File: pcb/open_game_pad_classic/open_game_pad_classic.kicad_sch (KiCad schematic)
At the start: 41 parts, among them J1 COM-09032, J2 COM-09032, U1 MM74C923, U2 74HC4051, U3 SN74AHC1G04DBVR, U4 LM358

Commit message: Updated the PCB and scheme. 2-layered, ground plane.
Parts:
- removed U4: LM358, LM358:DIL8, symbol Amplifier_Operational:LM358
- added AMP1: LM358, LM358:DIL8, symbol LM358:LM358
- C1: footprint Capacitor_SMD:C_0603_1608Metric -> Capacitor_SMD:C_0201_0603Metric
- C2, C3: footprint Capacitor_SMD:C_0402_1005Metric -> Capacitor_SMD:C_0201_0603Metric
- R1: footprint Resistor_SMD:R_0603_1608Metric -> Resistor_SMD:R_0402_1005Metric
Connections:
- net AIN: now also AMP1.1
- net at R10.2, R7.1: now also AMP1.2
- net at R8.2, R9.1: now also AMP1.3
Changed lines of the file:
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@@
 	)
 	(junction
+		(at 137.16 115.57)
+		(diameter 0)
+		(color 0 0 0 0)
+	)
+	(junction
 		(at 80.01 66.04)
 		(diameter 0)
@@
 	)
 	(junction
-		(at 137.16 115.57)
-		(diameter 0)
-		(color 0 0 0 0)
-	)
-	(junction
 		(at 60.96 121.92)
 		(diameter 0)
@@
 	)
 	(symbol
-		(lib_id "custom:SW_SPST_45_DEG")
-		(at 69.85 228.6 0)
+		(lib_id "LM358:LM358")
+		(at 129.54 115.57 0)
 		(unit 1)
 		(exclude_from_sim no)
@@
 		(dnp no)
 		(fields_autoplaced yes)
-		(property "Reference" "SW4"
-			(at 69.85 220.98 0)
+		(property "Reference" "AMP1"
+			(at 129.54 105.41 0)
 			(effects
 				(font
@@
 			)
 		)
-		(property "Value" "~"
-			(at 69.85 223.52 0)
+		(property "Value" "LM358"
+			(at 129.54 107.95 0)
 			(effects
 				(font
@@
 			)
 		)
-		(property "Footprint" "TS02-66-95-BK-260-LCR-D:SW_TS02-66-95-BK-260-LCR-D"
-			(at 69.85 228.6 0)
+		(property "Footprint" "LM358:DIL8"
+			(at 129.54 115.57 0)
 			(effects
 				(font
 					(size 1.27 1.27)
 				)
+				(justify bottom)
 				(hide yes)
 			)
 		)
-		(property "Datasheet" "~"
-			(at 69.85 228.6 0)
+		(property "Datasheet" ""
+			(at 129.54 115.57 0)
 			(effects
 				(font
@@
 			)
 		)
-		(property "Description" "Single Pole Single Throw (SPST) switch 45 deg"
-			(at 70.358 228.6 0)
+		(property "Description" ""
+			(at 129.54 115.57 0)
 			(effects
 				(font
@@
 			)
 		)
-		(pin "2"
+		(property "MF" "Texas Instruments"
+			(at 129.54 115.57 0)
+			(effects
+				(font
+					(size 1.27 1.27)
+				)
+				(justify bottom)
+				(hide yes)
+			)
 		)
-		(pin "1"
+		(property "Description_1" "\nOp Amp Dual Low Power Amplifier ±16V/32V 8-Pin TO-99 Tube\n"
+			(at 129.54 115.57 0)
+			(effects
+				(font
+					(size 1.27 1.27)
+				)
+				(justify bottom)
+				(hide yes)
+			)
 		)
-		(pin "3"
+		(property "Package" "None"
+			(at 129.54 115.57 0)
+			(effects
+				(font
+					(size 1.27 1.27)
+				)
+				(justify bottom)
+				(hide yes)
+			)
+		)
+		(property "Price" "None"
+			(at 129.54 115.57 0)
+			(effects
+				(font
+					(size 1.27 1.27)
+				)
+				(justify bottom)
+				(hide yes)
+			)
+		)
+		(property "SnapEDA_Link" "https://www.snapeda.com/parts/LM358/Texas+Instruments/view-part/?ref=snap"
+			(at 129.54 115.57 0)
+			(effects
+				(font
+					(size 1.27 1.27)
+				)
+				(justify bottom)
+				(hide yes)
+			)
+		)
+		(property "MP" "LM358"
+			(at 129.54 115.57 0)
+			(effects
+				(font
+					(size 1.27 1.27)
+				)
+				(justify bottom)
+				(hide yes)
+			)
+		)
+		(property "Purchase-URL" "https://www.snapeda.com/api/url_track_click_mouser/?unipart_id=11831622&manufacturer=Texas Instruments&part_name=LM358&search_term=None"
+			(at 129.54 115.57 0)
+			(effects
+				(font
+					(size 1.27 1.27)
+				)
+				(justify bottom)
+				(hide yes)
+			)
+		)
+		(property "Availability" "Not in stock"
+			(at 129.54 115.57 0)
+			(effects
+				(font
+					(size 1.27 1.27)
+				)
+				(justify bottom)
+				(hide yes)
+			)
+		)
+		(property "Check_prices" "https://www.snapeda.com/parts/LM358/Texas+Instruments/view-part/?ref=eda"
+			(at 129.54 115.57 0)
+			(effects
+				(font
+					(size 1.27 1.27)
+				)
+				(justify bottom)
+				(hide yes)
+			)
+		)
+		(pin "8"
 		)
 		(pin "4"
 		)
+		(pin "5"
+		)
+		(pin "6"
+		)
+		(pin "7"
+		)
+		(pin "1"
+		)
+		(pin "2"
+		)
+		(pin "3"
+		)
 		(instances
 			(project "open_game_pad_classic"
 				(path "/49f049bd-a8cc-4b05-820e-5d41d7ecc0be"
-					(reference "SW4")
+					(reference "AMP1")
 					(unit 1)
 				)
@@
 	(symbol
 		(lib_id "custom:SW_SPST_45_DEG")
-		(at 35.56 217.17 0)
+		(at 69.85 228.6 0)
 		(unit 1)
 		(exclude_from_sim no)
@@
 		(dnp no)
 		(fields_autoplaced yes)
-		(property "Reference" "SW5"
-			(at 35.56 209.55 0)
+		(property "Reference" "SW4"
+			(at 69.85 220.98 0)
 			(effects
 				(font
@@
 		)
 		(property "Value" "~"
-			(at 35.56 212.09 0)
+			(at 69.85 223.52 0)
 			(effects
 				(font
@@
 		)
 		(property "Footprint" "TS02-66-95-BK-260-LCR-D:SW_TS02-66-95-BK-260-LCR-D"
-			(at 35.56 217.17 0)
+			(at 69.85 228.6 0)
 			(effects
 				(font
@@
 		)
 		(property "Datasheet" "~"
-			(at 35.56 217.17 0)
+			(at 69.85 228.6 0)
 			(effects
 				(font
@@
 		)
 		(property "Description" "Single Pole Single Throw (SPST) switch 45 deg"
-			(at 36.068 217.17 0)
+			(at 70.358 228.6 0)
 			(effects
 				(font
@@
 		(pin "1"
 		)
-		(pin "4"
-		)
 		(pin "3"
 		)
+		(pin "4"
+		)
 		(instances
 			(project "open_game_pad_classic"
 				(path "/49f049bd-a8cc-4b05-820e-5d41d7ecc0be"
-					(reference "SW5")
+					(reference "SW4")
 					(unit 1)
 				)
@@
 	(symbol
 		(lib_id "custom:SW_SPST_45_DEG")
-		(at 46.99 205.74 0)
+		(at 35.56 217.17 0)
 		(unit 1)
 		(exclude_from_sim no)
@@
 		(dnp no)
 		(fields_autoplaced yes)
-		(property "Reference" "SW10"
-			(at 46.99 198.12 0)
+		(property "Reference" "SW5"
+			(at 35.56 209.55 0)
 			(effects
 				(font
@@
 		)
 		(property "Value" "~"
-			(at 46.99 200.66 0)
+			(at 35.56 212.09 0)
 			(effects
 				(font
@@
 		)
 		(property "Footprint" "TS02-66-95-BK-260-LCR-D:SW_TS02-66-95-BK-260-LCR-D"
-			(at 46.99 205.74 0)
+			(at 35.56 217.17 0)
 			(effects
 				(font
@@
 		)
 		(property "Datasheet" "~"
-			(at 46.99 205.74 0)
+			(at 35.56 217.17 0)
 			(effects
 				(font
@@
 		)
 		(property "Description" "Single Pole Single Throw (SPST) switch 45 deg"
-			(at 47.498 205.74 0)
+			(at 36.068 217.17 0)
 			(effects
 				(font
@@
 			(project "open_game_pad_classic"
 				(path "/49f049bd-a8cc-4b05-820e-5d41d7ecc0be"
-					(reference "SW10")
+					(reference "SW5")
 					(unit 1)
 				)
@@
 	(symbol
 		(lib_id "custom:SW_SPST_45_DEG")
-		(at 58.42 194.31 0)
+		(at 46.99 205.74 0)
 		(unit 1)
 		(exclude_from_sim no)
@@
 		(dnp no)
 		(fields_autoplaced yes)
-		(property "Reference" "SW15"
-			(at 58.42 186.69 0)
+		(property "Reference" "SW10"
+			(at 46.99 198.12 0)
 			(effects
 				(font
@@
 		)
 		(property "Value" "~"
-			(at 58.42 189.23 0)
+			(at 46.99 200.66 0)
 			(effects
 				(font
@@
 		)
 		(property "Footprint" "TS02-66-95-BK-260-LCR-D:SW_TS02-66-95-BK-260-LCR-D"
-			(at 58.42 194.31 0)
+			(at 46.99 205.74 0)
 			(effects
 				(font
@@
 		)
 		(property "Datasheet" "~"
-			(at 58.42 194.31 0)
+			(at 46.99 205.74 0)
 			(effects
 				(font
@@
 		)
 		(property "Description" "Single Pole Single Throw (SPST) switch 45 deg"
-			(at 58.928 194.31 0)
+			(at 47.498 205.74 0)
 			(effects
 				(font
@@
 			(project "open_game_pad_classic"
 				(path "/49f049bd-a8cc-4b05-820e-5d41d7ecc0be"
-					(reference "SW15")
+					(reference "SW10")
 					(unit 1)
 				)
@@
 	)
 	(symbol
-		(lib_id "Amplifier_Operational:LM358")
-		(at 129.54 115.57 0)
+		(lib_id "custom:SW_SPST_45_DEG")
+		(at 58.42 194.31 0)
 		(unit 1)
 		(exclude_from_sim no)
@@
 		(on_board yes)
 		(dnp no)
-		(property "Reference" "U4"
-			(at 129.54 105.41 0)
+		(fields_autoplaced yes)
+		(property "Reference" "SW15"
+			(at 58.42 186.69 0)
 			(effects
 				(font
@@
 			)
 		)
-		(property "Value" "LM358"
-			(at 129.54 107.95 0)
+		(property "Value" "~"
+			(at 58.42 189.23 0)
 			(effects
 				(font
@@
 			)
 		)
-		(property "Footprint" "LM358:DIL8"
-			(at 129.54 115.57 0)
+		(property "Footprint" "TS02-66-95-BK-260-LCR-D:SW_TS02-66-95-BK-260-LCR-D"
+			(at 58.42 194.31 0)
 			(effects
 				(font
@@
 			)
 		)
-		(property "Datasheet" "http://www.ti.com/lit/ds/symlink/lm2904-n.pdf"
-			(at 129.54 115.57 0)
+		(property "Datasheet" "~"
+			(at 58.42 194.31 0)
 			(effects
 				(font
@@
 			)
 		)
-		(property "Description" "Low-Power, Dual Operational Amplifiers, DIP-8/SOIC-8/TO-99-8"
-			(at 129.54 115.57 0)
+		(property "Description" "Single Pole Single Throw (SPST) switch 45 deg"
+			(at 58.928 194.31 0)
 			(effects
 				(font
@@
 			)
 		)
-		(pin "1"
-		)
-		(pin "8"
-		)
-		(pin "5"
-		)
-		(pin "3"
-		)
-		(pin "6"
-		)
 		(pin "2"
 		)
-		(pin "7"
+		(pin "1"
 		)
 		(pin "4"
 		)
+		(pin "3"
+		)
 		(instances
 			(project "open_game_pad_classic"
 				(path "/49f049bd-a8cc-4b05-820e-5d41d7ecc0be"
-					(reference "U4")
+					(reference "SW15")
 					(unit 1)
 				)
@@
 			)
 		)
-		(property "Footprint" "Capacitor_SMD:C_0402_1005Metric"
+		(property "Footprint" "Capacitor_SMD:C_0201_0603Metric"
 			(at 135.89 235.9152 0)
 			(effects
@@
 			)
 		)
-		(property "Footprint" "Resistor_SMD:R_0603_1608Metric"
+		(property "Footprint" "Resistor_SMD:R_0402_1005Metric"
 			(at 68.58 33.02 0)
 			(effects
@@
 			)
 		)
-		(property "Footprint" "Capacitor_SMD:C_0402_1005Metric"
+		(property "Footprint" "Capacitor_SMD:C_0201_0603Metric"
 			(at 127 238.4552 0)
 			(effects
@@
 			)
 		)
-		(property "Footprint" "Capacitor_SMD:C_0603_1608Metric"
+		(property "Footprint" "Capacitor_SMD:C_0201_0603Metric"
 			(at 167.3352 52.07 0)
 			(effects

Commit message: More decoupling for microcontroller and timer.
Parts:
- added C4: 10 pF, Capacitor_SMD:C_0201_0603Metric, symbol Device:C
- added C5: 10 µF, Capacitor_SMD:C_0603_1608Metric, symbol Device:C
- added C6: 100nF, Capacitor_SMD:C_0201_0603Metric, symbol Device:C
- C1: footprint Capacitor_SMD:C_0201_0603Metric -> Capacitor_SMD:C_0603_1608Metric
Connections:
- net +5V: now also C5.1, C6.1
- net CLK: now also C4.1
- net GND: now also C4.2, C5.2, C6.2
- no-connect marks 4 -> 5
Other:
- note added: "18 Tactile digital switch matrix."
- note removed: "15 Tactile digital switch matrix."
- moved on the sheet: C1

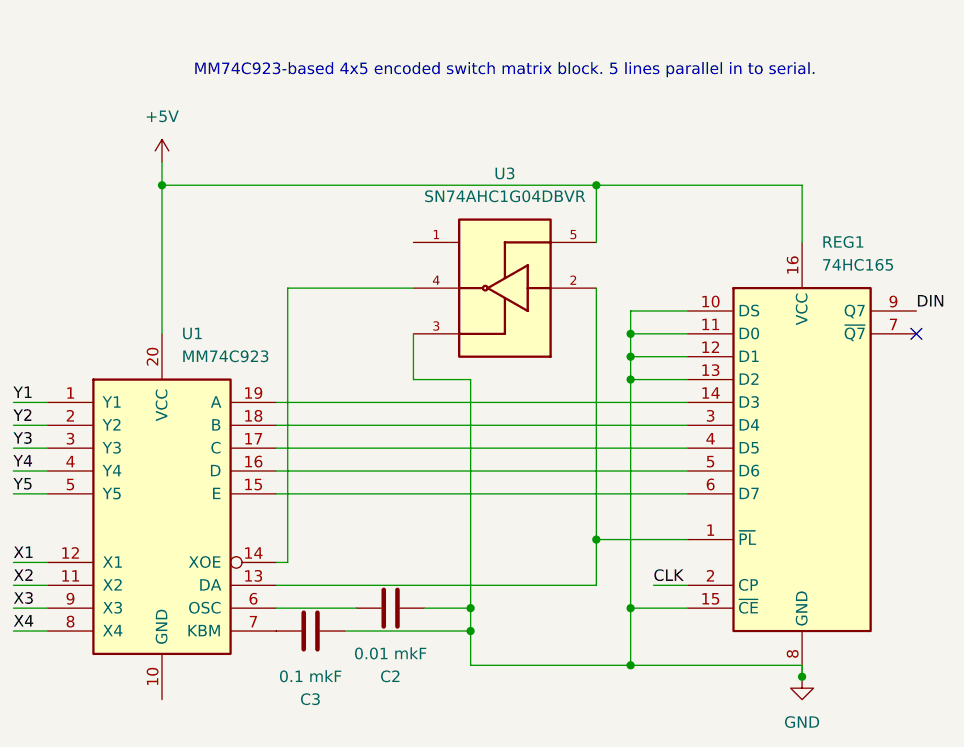
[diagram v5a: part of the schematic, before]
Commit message: Fixed the schematic on PISO read. Updated the PCB.
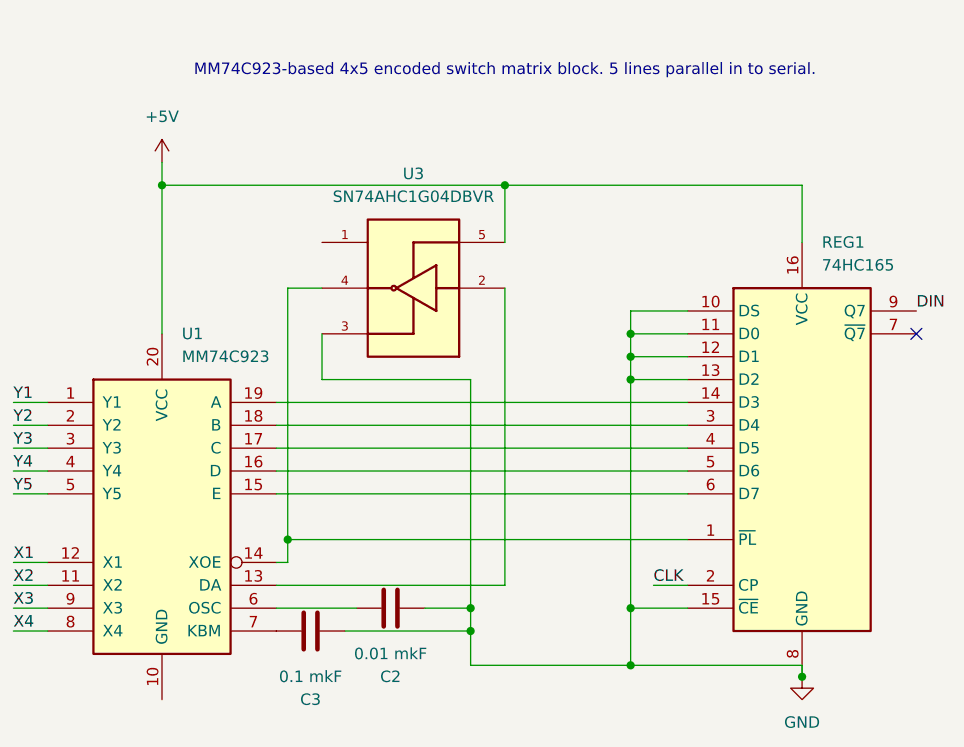
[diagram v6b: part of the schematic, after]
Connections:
- net at U1.13 (DA), U3.2: no longer REG1.1 (~{PL})
- net at U1.14 (XOE), U3.4: now also REG1.1 (~{PL})
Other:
- moved on the sheet: U3
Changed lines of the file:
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@@
 	)
 	(junction
-		(at 154.94 227.33)
-		(diameter 0)
-		(color 0 0 0 0)
-	)
-	(junction
 		(at 118.11 118.11)
 		(diameter 0)
@@
 	)
 	(junction
-		(at 140.97 234.95)
-		(diameter 0)
-		(color 0 0 0 0)
-	)
-	(junction
 		(at 74.93 231.14)
 		(diameter 0)
@@
 	)
 	(junction
+		(at 140.97 234.95)
+		(diameter 0)
+		(color 0 0 0 0)
+	)
+	(junction
 		(at 158.75 234.95)
 		(diameter 0)
@@
 	)
 	(junction
+		(at 144.78 187.96)
+		(diameter 0)
+		(color 0 0 0 0)
+	)
+	(junction
 		(at 40.64 219.71)
 		(diameter 0)
@@
 	)
 	(junction
+		(at 120.65 227.33)
+		(diameter 0)
+		(color 0 0 0 0)
+	)
+	(junction
 		(at 158.75 209.55)
 		(diameter 0)
@@
 	)
 	(junction
-		(at 154.94 187.96)
-		(diameter 0)
-		(color 0 0 0 0)
-	)
-	(junction
 		(at 76.2 135.89)
 		(diameter 0)
@@
 	(wire
 		(pts
-			(xy 106.68 187.96) (xy 154.94 187.96)
+			(xy 106.68 187.96) (xy 144.78 187.96)
 		)
 		(stroke
@@
 	(wire
 		(pts
-			(xy 140.97 209.55) (xy 140.97 234.95)
+			(xy 119.38 229.87) (xy 120.65 229.87)
 		)
 		(stroke
@@
 	(wire
 		(pts
-			(xy 119.38 229.87) (xy 120.65 229.87)
+			(xy 120.65 199.39) (xy 124.46 199.39)
 		)
 		(stroke
@@
 	(wire
 		(pts
-			(xy 120.65 199.39) (xy 134.62 199.39)
+			(xy 119.38 212.09) (xy 165.1 212.09)
 		)
 		(stroke
@@
 	(wire
 		(pts
-			(xy 119.38 212.09) (xy 165.1 212.09)
+			(xy 71.12 66.04) (xy 80.01 66.04)
 		)
 		(stroke
@@
 	(wire
 		(pts
-			(xy 71.12 66.04) (xy 80.01 66.04)
+			(xy 105.41 43.18) (xy 118.11 43.18)
 		)
 		(stroke
@@
 	(wire
 		(pts
-			(xy 105.41 43.18) (xy 118.11 43.18)
+			(xy 90.17 62.23) (xy 90.17 66.04)
 		)
 		(stroke
@@
 	(wire
 		(pts
-			(xy 90.17 62.23) (xy 90.17 66.04)
+			(xy 73.66 118.11) (xy 78.74 118.11)
 		)
 		(stroke
@@
 	(wire
 		(pts
-			(xy 73.66 118.11) (xy 78.74 118.11)
+			(xy 135.89 234.95) (xy 140.97 234.95)
 		)
 		(stroke
@@
 	(wire
 		(pts
-			(xy 140.97 209.55) (xy 134.62 209.55)
+			(xy 140.97 209.55) (xy 124.46 209.55)
 		)
 		(stroke
@@
 	(wire
 		(pts
-			(xy 63.5 153.67) (xy 49.53 153.67)
+			(xy 120.65 227.33) (xy 165.1 227.33)
 		)
 		(stroke
@@
 	(wire
 		(pts
-			(xy 180.34 125.73) (xy 180.34 123.19)
+			(xy 63.5 153.67) (xy 49.53 153.67)
 		)
 		(stroke
@@
 	(wire
 		(pts
-			(xy 111.76 91.44) (xy 111.76 102.87)
+			(xy 180.34 125.73) (xy 180.34 123.19)
 		)
 		(stroke
@@
 	(wire
 		(pts
-			(xy 135.89 234.95) (xy 140.97 234.95)
+			(xy 111.76 91.44) (xy 111.76 102.87)
 		)
 		(stroke
@@
 	(wire
 		(pts
-			(xy 120.65 229.87) (xy 120.65 199.39)
+			(xy 120.65 229.87) (xy 120.65 227.33)
 		)
 		(stroke
@@
 	(wire
 		(pts
-			(xy 154.94 227.33) (xy 165.1 227.33)
+			(xy 90.17 45.72) (xy 92.71 45.72)
 		)
 		(stroke
@@
 	(wire
 		(pts
-			(xy 90.17 45.72) (xy 92.71 45.72)
+			(xy 49.53 104.14) (xy 71.12 104.14)
 		)
 		(stroke
@@
 	(wire
 		(pts
-			(xy 49.53 104.14) (xy 71.12 104.14)
+			(xy 140.97 234.95) (xy 140.97 237.49)
 		)
 		(stroke
@@
 	(wire
 		(pts
-			(xy 140.97 234.95) (xy 140.97 237.49)
+			(xy 80.01 40.64) (xy 66.04 40.64)
 		)
 		(stroke
@@
 	(wire
 		(pts
-			(xy 80.01 40.64) (xy 66.04 40.64)
+			(xy 63.5 208.28) (xy 63.5 219.71)
 		)
 		(stroke
@@
 	(wire
 		(pts
-			(xy 63.5 208.28) (xy 63.5 219.71)
+			(xy 140.97 209.55) (xy 140.97 234.95)
 		)
 		(stroke
@@
 	(wire
 		(pts
+			(xy 144.78 187.96) (xy 177.8 187.96)
+		)
+		(stroke
+			(width 0)
+			(type default)
+		)
+	)
+	(wire
+		(pts
 			(xy 158.75 241.3) (xy 177.8 241.3)
 		)
@@
 	(wire
 		(pts
-			(xy 154.94 199.39) (xy 154.94 227.33)
-		)
-		(stroke
-			(width 0)
-			(type default)
-		)
-	)
-	(wire
-		(pts
 			(xy 63.5 196.85) (xy 63.5 208.28)
 		)
@@
 	(wire
 		(pts
-			(xy 154.94 187.96) (xy 177.8 187.96)
-		)
-		(stroke
-			(width 0)
-			(type default)
-		)
-	)
-	(wire
-		(pts
 			(xy 119.38 222.25) (xy 165.1 222.25)
 		)
@@
 	(wire
 		(pts
-			(xy 154.94 227.33) (xy 154.94 232.41)
+			(xy 144.78 199.39) (xy 144.78 232.41)
 		)
 		(stroke
@@
 	(wire
 		(pts
+			(xy 120.65 227.33) (xy 120.65 199.39)
+		)
+		(stroke
+			(width 0)
+			(type default)
+		)
+	)
+	(wire
+		(pts
 			(xy 133.35 66.04) (xy 133.35 60.96)
 		)
@@
 	(wire
 		(pts
-			(xy 154.94 187.96) (xy 154.94 194.31)
+			(xy 144.78 187.96) (xy 144.78 194.31)
 		)
 		(stroke
@@
 	(wire
 		(pts
-			(xy 119.38 232.41) (xy 154.94 232.41)
+			(xy 119.38 232.41) (xy 144.78 232.41)
 		)
 		(stroke
@@
 	(wire
 		(pts
-			(xy 134.62 209.55) (xy 134.62 204.47)
+			(xy 124.46 209.55) (xy 124.46 204.47)
 		)
 		(stroke
@@
 	(symbol
 		(lib_id "SN74AHC1G04DBVR:SN74AHC1G04DBVR")
-		(at 144.78 199.39 0)
+		(at 134.62 199.39 0)
 		(mirror y)
 		(unit 1)
@@
 		(dnp no)
 		(property "Reference" "U3"
-			(at 144.78 186.69 0)
+			(at 134.62 186.69 0)
 			(effects
 				(font
@@
 		)
 		(property "Value" "SN74AHC1G04DBVR"
-			(at 144.78 189.23 0)
+			(at 134.62 189.23 0)
 			(effects
 				(font
@@
 		)
 		(property "Footprint" "SN74AHC1G04DBVR:SOT95P280X145-5N"
-			(at 144.78 199.39 0)
+			(at 134.62 199.39 0)
 			(effects
 				(font
@@
 		)
 		(property "Datasheet" ""
-			(at 144.78 199.39 0)
+			(at 134.62 199.39 0)
 			(effects
 				(font
@@
 		)
 		(property "Description" ""
-			(at 144.78 199.39 0)
+			(at 134.62 199.39 0)
 			(effects
 				(font
@@
 		)
 		(property "MF" "Texas Instruments"
-			(at 144.78 199.39 0)
+			(at 134.62 199.39 0)
 			(effects
 				(font
@@
 		)
 		(property "MAXIMUM_PACKAGE_HEIGHT" "1.45mm"
-			(at 144.78 199.39 0)
+			(at 134.62 199.39 0)
 			(effects
 				(font
@@
 		)
 		(property "Package" "SOT-23-5 Texas Instruments"
-			(at 144.78 199.39 0)
+			(at 134.62 199.39 0)
 			(effects
 				(font
@@
 		)
 		(property "Price" "None"
-			(at 144.78 199.39 0)
+			(at 134.62 199.39 0)
 			(effects
 				(font
@@
 		)
 		(property "Check_prices" "https://www.snapeda.com/parts/SN74AHC1G04DBVR/Texas+Instruments/view-part/?ref=eda"
-			(at 144.78 199.39 0)
+			(at 134.62 199.39 0)
 			(effects
 				(font
@@
 		)
 		(property "STANDARD" "IPC-7351B"
-			(at 144.78 199.39 0)
+			(at 134.62 199.39 0)
 			(effects
 				(font
@@
 		)
 		(property "PARTREV" "AD"
-			(at 144.78 199.39 0)
+			(at 134.62 199.39 0)
 			(effects
 				(font
@@
 		)
 		(property "SnapEDA_Link" "https://www.snapeda.com/parts/SN74AHC1G04DBVR/Texas+Instruments/view-part/?ref=snap"
-			(at 144.78 199.39 0)
+			(at 134.62 199.39 0)
 			(effects
 				(font
@@
 		)
 		(property "MP" "SN74AHC1G04DBVR"
-			(at 144.78 199.39 0)
+			(at 134.62 199.39 0)
 			(effects
 				(font
@@
 		)
 		(property "Description_1" "\nSingle 2-V to 5.5-V inverter\n"
-			(at 144.78 199.39 0)
+			(at 134.62 199.39 0)
 			(effects
 				(font
@@
 		)
 		(property "Availability" "In Stock"
-			(at 144.78 199.39 0)
+			(at 134.62 199.39 0)
 			(effects
 				(font
@@
 		)
 		(property "MANUFACTURER" "Texas Instruments"
-			(at 144.78 199.39 0)
+			(at 134.62 199.39 0)
 			(effects
 				(font

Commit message: Fixed the reset problem by adding an 8-tick delay.
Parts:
- removed U3: SN74AHC1G04DBVR, SN74AHC1G04DBVR:SOT95P280X145-5N, symbol SN74AHC1G04DBVR:SN74AHC1G04DBVR
- added U3: 74AHC1G00, Package_TO_SOT_SMD:SOT-23-5, symbol 74xGxx:74AHC1G00
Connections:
- net +5V: now also U3.5 (VCC)
- net GND: now also U3.3 (GND); no longer REG1.11 (D0)
- net 8TICK: now reaches CR1.11 (Q3)
- net 8TICK: now also U3.1
- net at U1.13 (DA): now also REG1.11 (D0), U3.2
- net at REG1.1 (~{PL}), U1.14 (XOE): now also U3.4
- no-connect marks 5 -> 4
